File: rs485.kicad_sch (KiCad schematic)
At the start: 7 parts, among them U7 ISL3172EIUZ

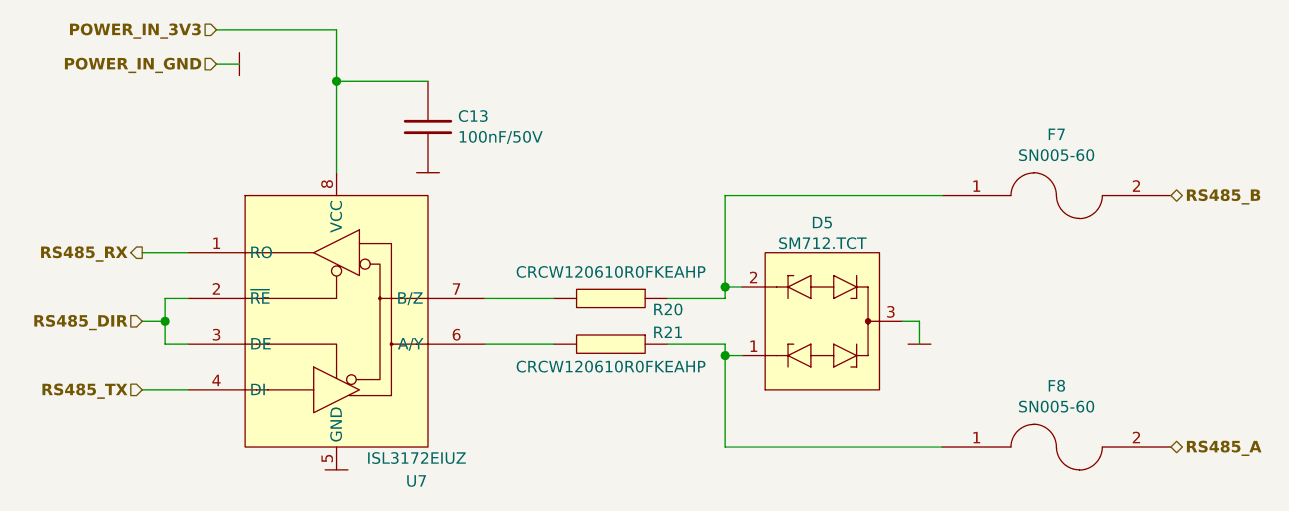
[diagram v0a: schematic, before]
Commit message: created new layout for adjusted schematic
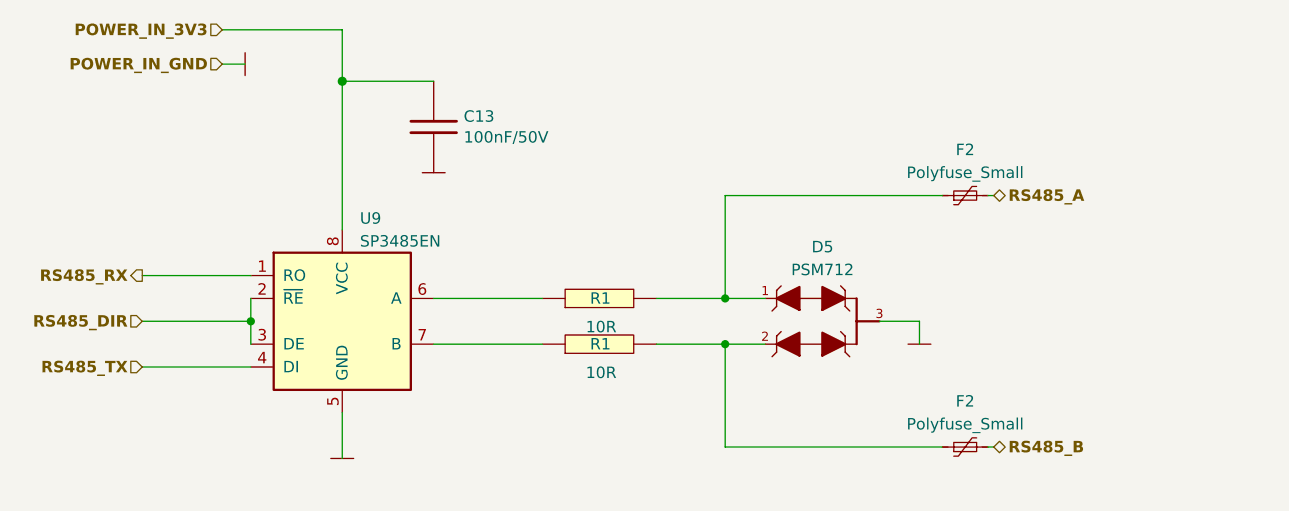
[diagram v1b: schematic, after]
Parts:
- removed D5: SM712.TCT, ESD_Protectors:SM712.TCT, symbol esd_protectors:SM712.TCT
- removed F7, F8: SN005-60, Smd_Ptc_Fuses:SN005-60, symbol Ptc_Smd_Fuses:SN005-60
- removed R20, R21: CRCW120610R0FKEAHP, Resistor_Smd_1206:CRCW120610R0FKEAHP, symbol Resistors_Smd1206:CRCW120610R0FKEAHP
- removed U7: ISL3172EIUZ, Communication_Interfaces:ISL3172EIUZ, symbol Communication_Interfaces:ISL3172EIUZ
- added D5: PSM712, PSM712:SOT23-3, symbol PSM712:PSM712
- added F2 (x2): Polyfuse_Small, Fuse:Fuse_1206_3216Metric, symbol Device:Polyfuse_Small
- added R1 (x2): 10R, Resistor_SMD:R_1206_3216Metric, symbol Resistors_Smd0805:60.4R
- added U9: SP3485EN, Package_SO:SOIC-8_3.9x4.9mm_P1.27mm, symbol Interface_UART:SP3485EN
- C13: footprint Capacitors_Smd_0603:100nF_0603 -> Capacitor_SMD:C_0603_1608Metric
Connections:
- net GND: now also D5.3, U9.5 (GND)
- net POWER_IN_3V3: now also U9.8 (VCC)
- net RS485_A: now also F2.2
- net RS485_B: now also F2.2
- net RS485_DIR: now also U9.2 (~{RE}), U9.3 (DE)
- net RS485_RX: now also U9.1 (RO)
- net RS485_TX: now also U9.4 (DI)
- new net: R1.1, U9.6 (A)
- new net: D5.1, F2.1, R1.2
- new net: D5.2, F2.1, R1.2
- new net: R1.1, U9.7 (B)
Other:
- moved on the sheet: C13
